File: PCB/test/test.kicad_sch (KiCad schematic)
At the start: 56 parts, among them CN1 HEADER_1X10, CN3 USB_1, CN4 HEADER_1X4, CN5 UFL, SW2 MLL1200S_TE, U1 STM32WBxx_QFN48, U2 USBLC6-2SC6, U3 LD3985M33R, X1 NX2016_32MHz, X2 NX2012_32K768Hz

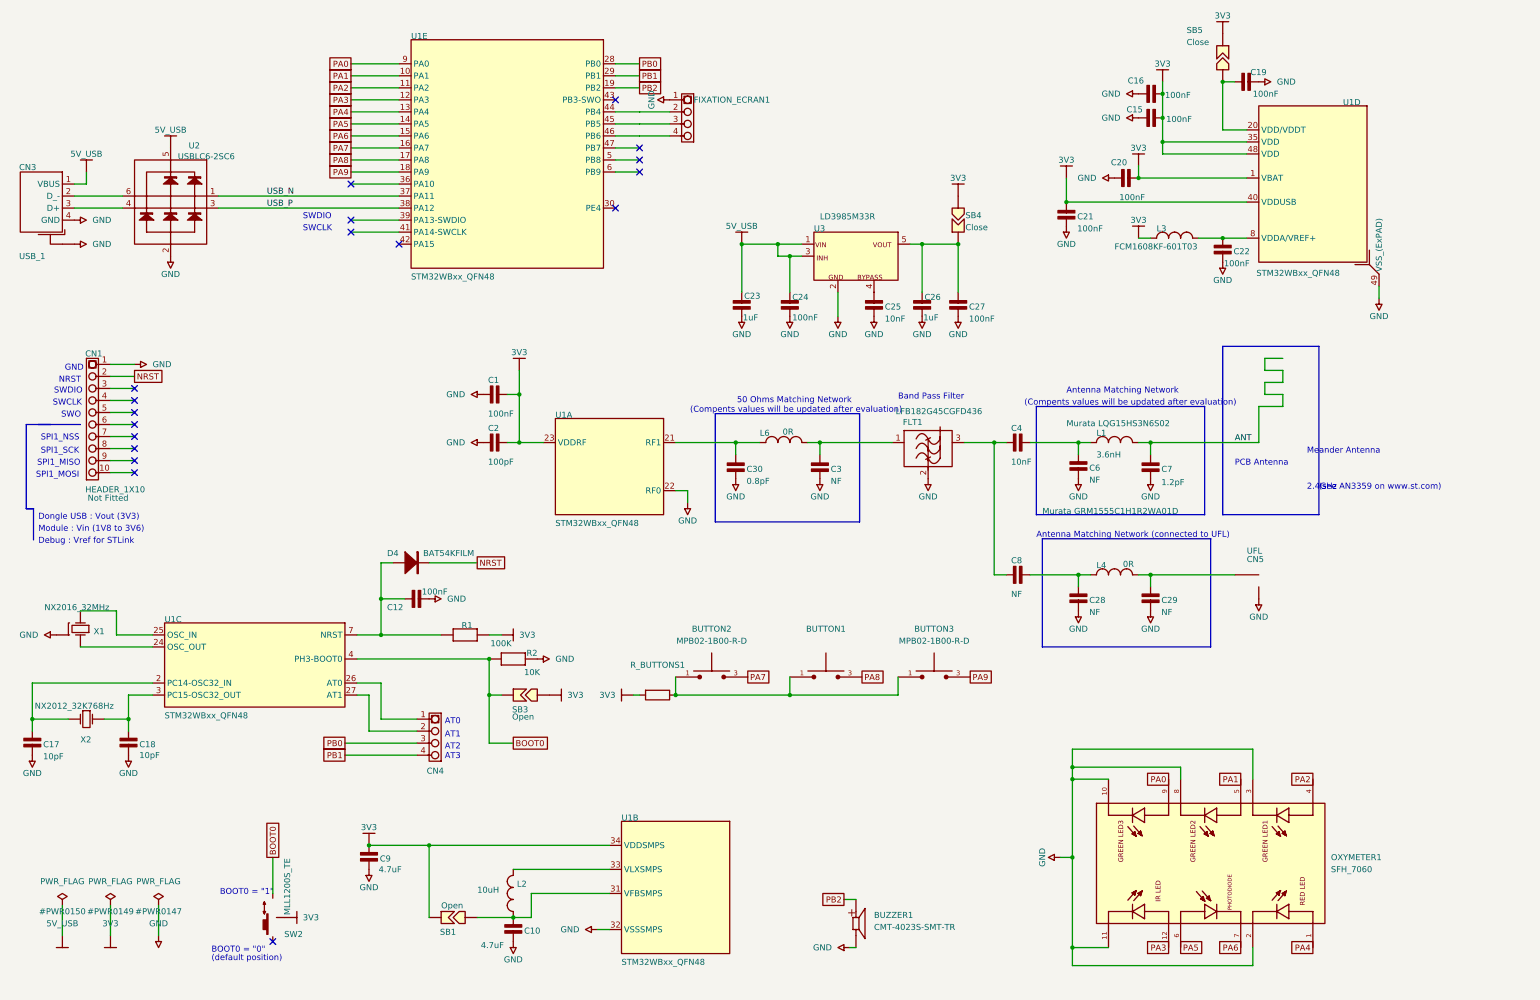
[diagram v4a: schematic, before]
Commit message: changement nrst
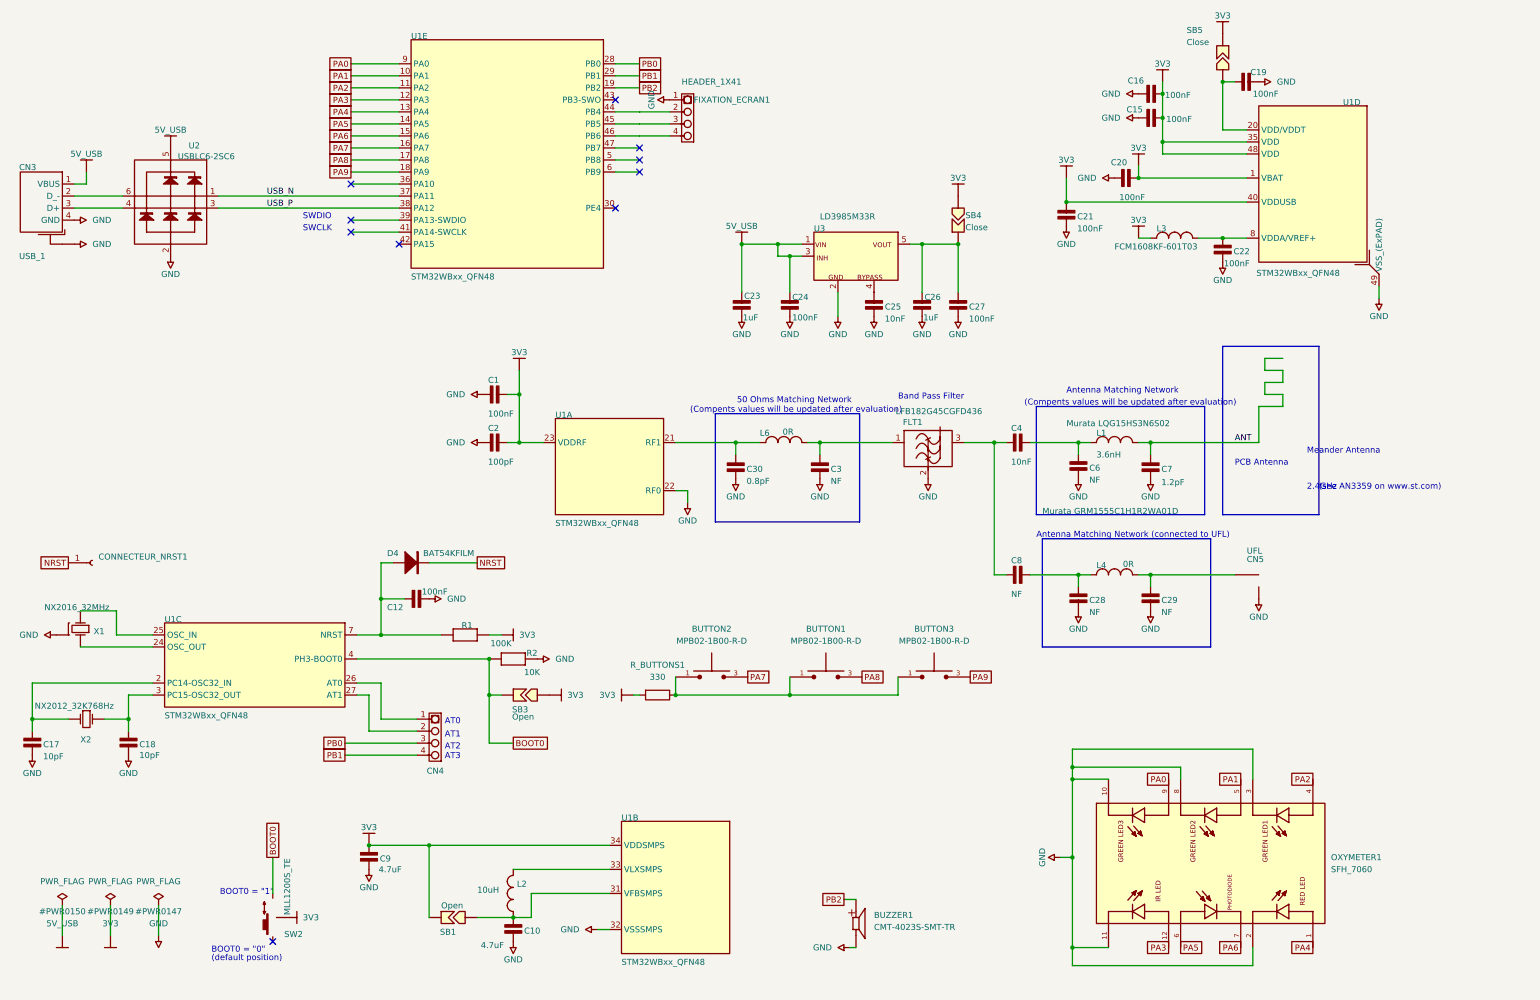
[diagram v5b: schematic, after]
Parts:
- removed CN1: HEADER_1X10, Header M/F 1x10x2.54 NF, symbol test-altium-import:0_HEADER_1X10
- added CONNECTEUR_NRST1: (no value), symbol Connector:Conn_01x01_Female
- BUTTON1: value (none) -> MPB02-1B00-R-D; footprint (none) -> SW_MPB02-1B00-R-D
- FIXATION_ECRAN1: value (none) -> HEADER_1X41
- R_BUTTONS1: value (none) -> 330
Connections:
- net NRST: now also CONNECTEUR_NRST1.1 (Pin_1)
- no-connect marks 18 -> 10
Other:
- note removed: "Debug : Vref for STLink"
- note removed: "Dongle USB : Vout (3V3)"
- note removed: "GND"
- note removed: "Module : Vin (1V8 to 3V6)"
- note removed: "NRST"
- note removed: "SPI1_MISO"
- note removed: "SPI1_MOSI"
- note removed: "SPI1_NSS"
- note removed: "SPI1_SCK"
- note removed: "SWO"

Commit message: génération netlist
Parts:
- CN3: footprint USB/A_M1 -> (none)
- CONNECTEUR_NRST1: value (none) -> Conn_01x01_Female
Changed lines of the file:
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@@
       (effects (font (size 1.27 1.27)) (justify left))
     )
-    (property "Value" "" (id 1) (at 19.05 119.3799 0)
+    (property "Value" "Conn_01x01_Female" (id 1) (at 19.05 119.3799 0)
       (effects (font (size 1.27 1.27)) (justify left))
     )
@@
   )
   (symbol (lib_id "MPB02-1B00-R-D:MPB02-1B00-R-D") (at 148.59 142.24 0) (unit 1)
-    (in_bom yes) (on_board yes) (fields_autoplaced)
+    (in_bom yes) (on_board yes)
     (property "Reference" "BUTTON2" (id 0) (at 148.59 132.08 0))
     (property "Value" "MPB02-1B00-R-D" (id 1) (at 148.59 134.62 0))
-    (property "Footprint" "SW_MPB02-1B00-R-D" (id 2) (at 148.59 142.24 0)
-      (effects (font (size 1.27 1.27)) (justify left bottom) hide)
+    (property "Footprint" "SW_MPB02-1B00-R-D" (id 2) (at 138.43 130.81 0)
+      (effects (font (size 1.27 1.27)) (justify left bottom))
     )
     (property "Datasheet" "" (id 3) (at 148.59 142.24 0)
@@
       (effects (font (size 1.27 1.27)) (justify left bottom))
     )
-    (property "Footprint" "USB/A_M1" (id 2) (at 11.43 43.18 0)
+    (property "Footprint" "" (id 2) (at 11.43 43.18 0)
       (effects (font (size 1.27 1.27)) hide)
     )
@@
     )
     (path "/f1447ad6-651c-45be-a2d6-33bddf672c2c"
-      (reference "CN3") (unit 1) (value "USB_1") (footprint "USB/A_M1")
+      (reference "CN3") (unit 1) (value "USB_1") (footprint "USB_A_M1")
     )
     (path "/12fa3c3f-3d14-451a-a6a8-884fd1b32fa7"
@@
     )
     (path "/2713445a-5e01-40d8-94c6-c4d9a94c1daa"
-      (reference "CONNECTEUR_NRST1") (unit 1) (value "Conn_01x01_Female") (footprint "")
+      (reference "CONNECTEUR_NRST1") (unit 1) (value "Conn_01x01_Female") (footprint "Connector_PinHeader_2.54mm:PinHeader_1x01_P2.54mm_Vertical")
     )
     (path "/810ed4ff-ffe2-4032-9af6-fb5ada3bae5b"
@@
     )
     (path "/861921d0-f23c-4ac4-a1dd-b8dca74aec48"
-      (reference "FIXATION_ECRAN1") (unit 1) (value "HEADER_1X41") (footprint "")
+      (reference "FIXATION_ECRAN1") (unit 1) (value "HEADER_1X41") (footprint "Connector_PinHeader_2.54mm:PinHeader_1x04_P2.54mm_Vertical")
     )
     (path "/186c3f1e-1c94-498e-abf2-1069980f6633"
@@
     )
     (path "/df25edc2-4eb2-42fb-ac81-7e026ff7e840"
-      (reference "R_BUTTONS1") (unit 1) (value "330") (footprint "")
+      (reference "R_BUTTONS1") (unit 1) (value "330") (footprint "Resistor_SMD:R_0402_1005Metric")
     )
     (path "/51cc007a-3378-4ce3-909c-71e94822f8d1"

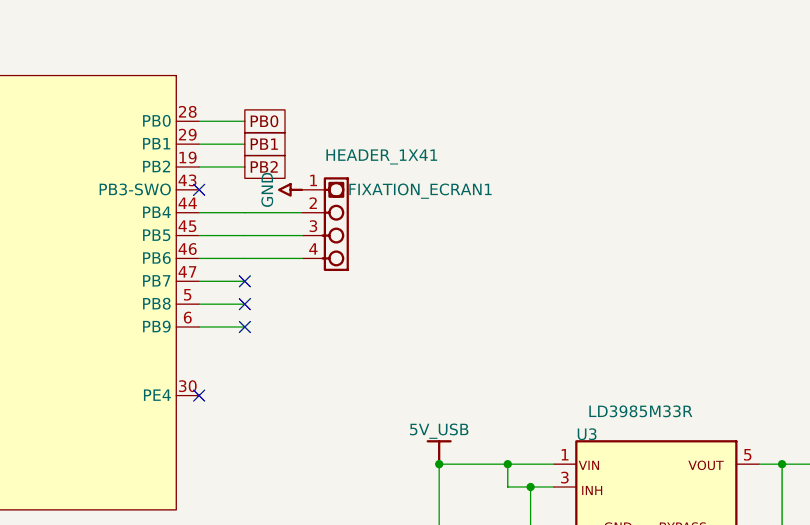
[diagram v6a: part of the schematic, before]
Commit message: ajout de footprints
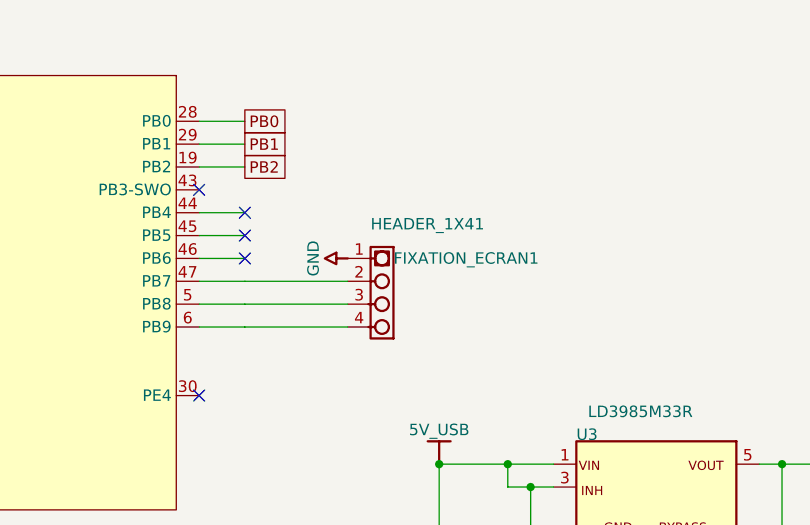
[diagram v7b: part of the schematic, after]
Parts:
- CN3: footprint (none) -> USB_A_M1
- CONNECTEUR_NRST1: footprint (none) -> Connector_PinHeader_2.54mm:PinHeader_1x01_P2.54mm_Vertical
- FIXATION_ECRAN1: footprint (none) -> Connector_PinHeader_2.54mm:PinHeader_1x04_P2.54mm_Vertical
- R_BUTTONS1: footprint (none) -> Resistor_SMD:R_0402_1005Metric
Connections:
- net at U1.44 (PB4): no longer FIXATION_ECRAN1.2
- net at U1.45 (PB5): no longer FIXATION_ECRAN1.3
- net at U1.46 (PB6): no longer FIXATION_ECRAN1.4
- net at U1.47 (PB7): now also FIXATION_ECRAN1.2
- net at U1.5 (PB8): now also FIXATION_ECRAN1.3
- net at U1.6 (PB9): now also FIXATION_ECRAN1.4
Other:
- moved on the sheet: FIXATION_ECRAN1
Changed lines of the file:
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@@
   )
   (no_connect (at 55.88 198.12))
-  (no_connect (at 133.35 33.02))
-  (no_connect (at 133.35 35.56))
+  (no_connect (at 133.35 22.86))
   (no_connect (at 128.27 43.18))
   (no_connect (at 72.39 38.1))
   (no_connect (at 128.27 20.32))
   (no_connect (at 72.39 45.72))
-  (no_connect (at 133.35 30.48))
+  (no_connect (at 133.35 27.94))
   (no_connect (at 72.39 48.26))
   (no_connect (at 82.55 50.8))
+  (no_connect (at 133.35 25.4))
   (wire (pts (xy 256.54 16.51) (xy 256.54 26.67))
     (stroke (width 0.254) (type default) (color 0 0 0 0))
@@
     (stroke (width 0.254) (type default) (color 0 0 0 0))
   )
+  (wire (pts (xy 133.35 33.02) (xy 144.78 33.02))
+    (stroke (width 0) (type default) (color 0 0 0 0))
+  )
   (wire (pts (xy 128.27 35.56) (xy 133.35 35.56))
     (stroke (width 0.254) (type default) (color 0 0 0 0))
@@
     (stroke (width 0.254) (type default) (color 0 0 0 0))
   )
+  (wire (pts (xy 133.35 30.48) (xy 144.78 30.48))
+    (stroke (width 0) (type default) (color 0 0 0 0))
+  )
   (wire (pts (xy 223.52 41.91) (xy 223.52 36.83))
     (stroke (width 0.254) (type default) (color 0 0 0 0))
@@
     (stroke (width 0.254) (type default) (color 0 0 0 0))
   )
+  (wire (pts (xy 133.35 35.56) (xy 144.78 35.56))
+    (stroke (width 0) (type default) (color 0 0 0 0))
+  )
   (wire (pts (xy 25.4 151.13) (xy 20.32 151.13))
     (stroke (width 0.254) (type default) (color 0 0 0 0))
@@
     (stroke (width 0.254) (type default) (color 0 0 0 0))
   )
-  (wire (pts (xy 133.35 22.86) (xy 139.7 22.86))
-    (stroke (width 0) (type default) (color 0 0 0 0))
-  )
   (wire (pts (xy 165.1 60.96) (xy 165.1 53.34))
     (stroke (width 0.254) (type default) (color 0 0 0 0))
@@
     (stroke (width 0.254) (type default) (color 0 0 0 0))
   )
-  (wire (pts (xy 133.35 25.4) (xy 139.7 25.4))
-    (stroke (width 0) (type default) (color 0 0 0 0))
-  )
   (polyline (pts (xy 254 113.03) (xy 218.44 113.03))
     (stroke (width 0) (type solid) (color 0 0 0 0))
@@
   (wire (pts (xy 241.3 120.65) (xy 259.08 120.65))
     (stroke (width 0.254) (type default) (color 0 0 0 0))
-  )
-  (wire (pts (xy 133.35 27.94) (xy 139.7 27.94))
-    (stroke (width 0) (type default) (color 0 0 0 0))
   )
   (wire (pts (xy 247.65 163.83) (xy 247.65 161.29))
@@
       (effects (font (size 1.27 1.27)) (justify left))
     )
-    (property "Footprint" "" (id 2) (at 17.78 118.11 0)
+    (property "Footprint" "Connector_PinHeader_2.54mm:PinHeader_1x01_P2.54mm_Vertical" (id 2) (at 17.78 118.11 0)
       (effects (font (size 1.27 1.27)) hide)
     )
@@
     (pin "4")
   )
-  (symbol (lib_id "test-altium-import:GND") (at 139.7 20.32 270) (unit 1)
-    (in_bom yes) (on_board yes)
-    (property "Reference" "#PWR0155" (id 0) (at 139.7 20.32 0)
-      (effects (font (size 1.27 1.27)) hide)
-    )
-    (property "Value" "GND" (id 1) (at 135.89 20.32 0))
-    (property "Footprint" "" (id 2) (at 139.7 20.32 0)
-      (effects (font (size 1.27 1.27)) hide)
-    )
-    (property "Datasheet" "" (id 3) (at 139.7 20.32 0)
+  (symbol (lib_id "test-altium-import:GND") (at 144.78 27.94 270) (unit 1)
+    (in_bom yes) (on_board yes)
+    (property "Reference" "#PWR0155" (id 0) (at 144.78 27.94 0)
+      (effects (font (size 1.27 1.27)) hide)
+    )
+    (property "Value" "GND" (id 1) (at 140.97 27.94 0))
+    (property "Footprint" "" (id 2) (at 144.78 27.94 0)
+      (effects (font (size 1.27 1.27)) hide)
+    )
+    (property "Datasheet" "" (id 3) (at 144.78 27.94 0)
       (effects (font (size 1.27 1.27)) hide)
     )
@@
     (pin "9")
   )
-  (symbol (lib_id "test-altium-import:0_mirrored_HEADER_1X4") (at 137.16 27.94 0) (unit 1)
-    (in_bom yes) (on_board yes)
-    (property "Reference" "FIXATION_ECRAN1" (id 0) (at 144.78 20.32 0)
+  (symbol (lib_id "test-altium-import:0_mirrored_HEADER_1X4") (at 142.24 35.56 0) (unit 1)
+    (in_bom yes) (on_board yes)
+    (property "Reference" "FIXATION_ECRAN1" (id 0) (at 149.86 27.94 0)
       (effects (font (size 1.27 1.27)) (justify left))
     )
-    (property "Value" "HEADER_1X41" (id 1) (at 142.24 16.51 0)
+    (property "Value" "HEADER_1X41" (id 1) (at 147.32 24.13 0)
       (effects (font (size 1.27 1.27)) (justify left))
     )
-    (property "Footprint" "" (id 2) (at 137.16 27.94 0)
-      (effects (font (size 1.27 1.27)) hide)
-    )
-    (property "Datasheet" "" (id 3) (at 137.16 27.94 0)
+    (property "Footprint" "Connector_PinHeader_2.54mm:PinHeader_1x04_P2.54mm_Vertical" (id 2) (at 142.24 35.56 0)
+      (effects (font (size 1.27 1.27)) hide)
+    )
+    (property "Datasheet" "" (id 3) (at 142.24 35.56 0)
       (effects (font (size 1.27 1.27)) hide)
     )
@@
     (property "Reference" "R_BUTTONS1" (id 0) (at 137.16 139.7 90))
     (property "Value" "330" (id 1) (at 137.16 142.24 90))
-    (property "Footprint" "" (id 2) (at 137.16 144.272 90)
+    (property "Footprint" "Resistor_SMD:R_0402_1005Metric" (id 2) (at 137.16 144.272 90)
       (effects (font (size 1.27 1.27)) hide)
     )
@@
       (effects (font (size 1.27 1.27)) (justify left bottom))
     )
-    (property "Footprint" "" (id 2) (at 11.43 43.18 0)
-      (effects (font (size 1.27 1.27)) hide)
-    )
+    (property "Footprint" "USB_A_M1" (id 2) (at 11.43 43.18 0)
+      (effects (font (size 1.27 1.27)) hide)
+    )
